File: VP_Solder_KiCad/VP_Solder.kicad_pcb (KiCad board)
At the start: 2 copper layers, 281 x 94.4 mm, 169 parts, among them J1 Conn_01x04, SW1 SW_Push, SW2 SW_Push, U1 STM32F072CBTx, U2 XC6206PxxxMR, U3 USBLC6-2SC6

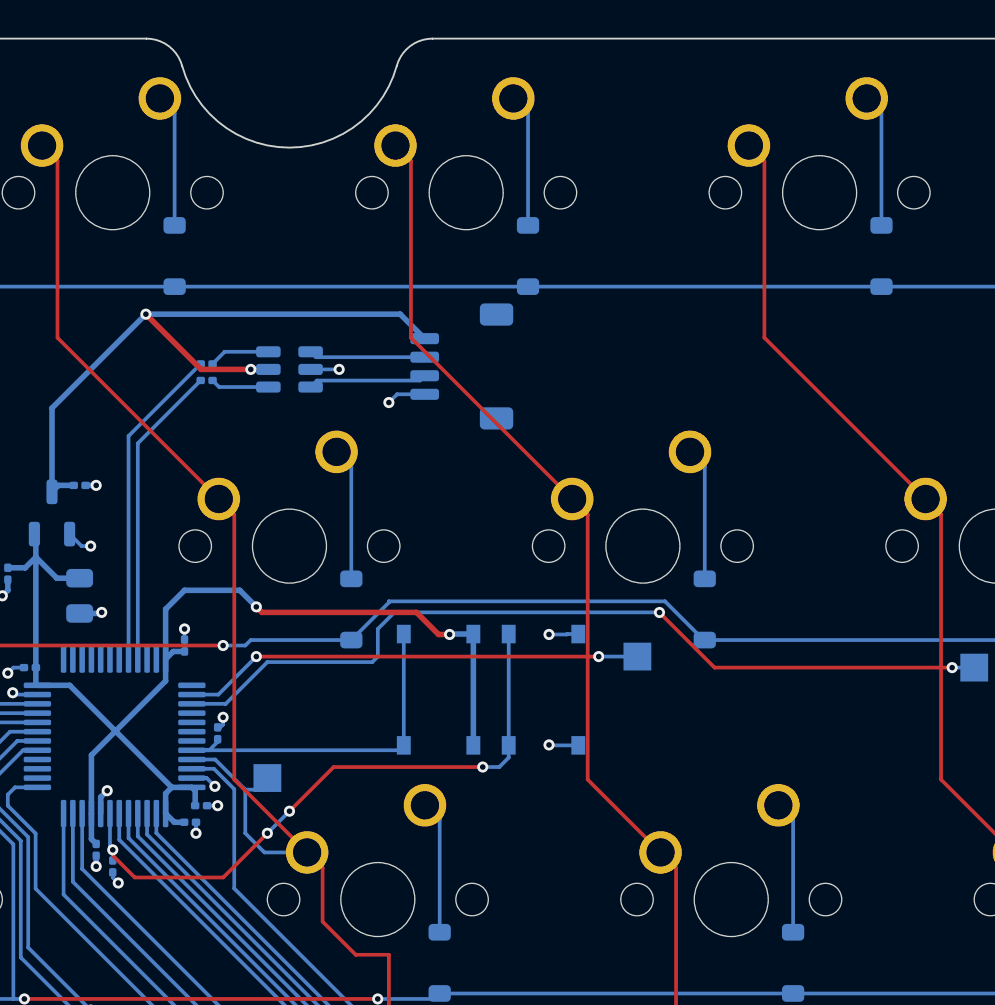
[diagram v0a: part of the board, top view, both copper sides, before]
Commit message: Small changes to silkscreen
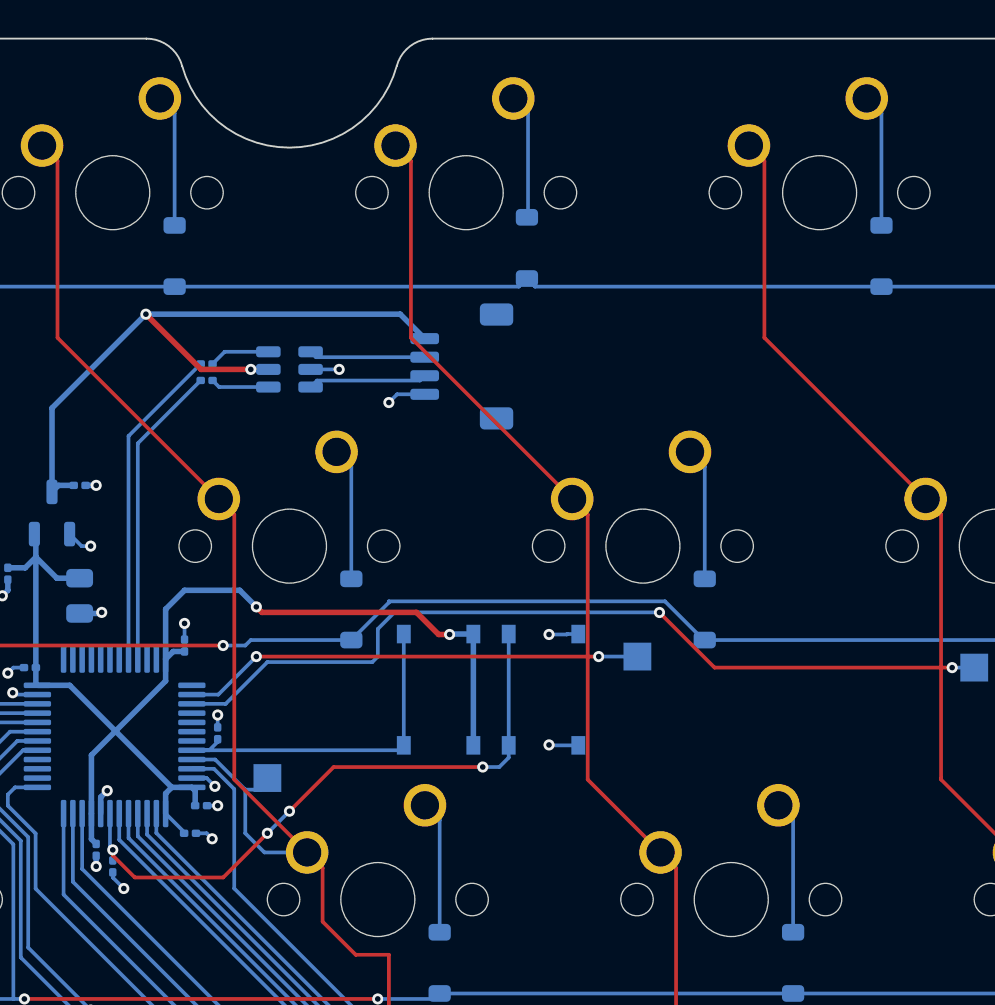
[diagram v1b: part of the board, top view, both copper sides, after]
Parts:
- added G***: LOGO, LOGO, B.Cu at (168.8, 151.3)
- moved C1 0.60 mm to (104.2, 113.0)
- moved D3 0.44 mm to (122.3, 81.4)
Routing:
- net GND: track 19.9 -> 21.0 mm
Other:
- board text added: "Firmware:"

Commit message: Changed testpoint names
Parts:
- renumbered TP2 to COL0, TP3 to COL1, TP12 to COL10, TP13 to COL11, TP14 to COL12, TP15 to COL13, TP4 to COL2, TP5 to COL3, TP6 to COL4, TP7 to COL5, TP8 to COL6, TP9 to COL7, TP10 to COL8, TP11 to COL9, TP1 to GND1
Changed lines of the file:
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@@
 		(descr "SMD rectangular pad as test Point, square 1.5mm side length")
 		(tags "test point SMD pad rectangle square")
-		(property "Reference" "TP4"
+		(property "Reference" "COL2"
 			(at 0 -1.785725 0)
 			(layer "B.SilkS")
@@
 		(descr "SMD rectangular pad as test Point, square 1.5mm side length")
 		(tags "test point SMD pad rectangle square")
-		(property "Reference" "TP3"
-			(at -2.381298 0.000203 0)
+		(property "Reference" "COL1"
+			(at -2.97656 0.000203 0)
 			(layer "B.SilkS")
 			(effects
@@
 		(descr "SMD rectangular pad as test Point, square 1.5mm side length")
 		(tags "test point SMD pad rectangle square")
-		(property "Reference" "TP13"
+		(property "Reference" "COL11"
 			(at -0.000337 -1.785762 0)
 			(layer "B.SilkS")
@@
 		(descr "SMD rectangular pad as test Point, square 1.5mm side length")
 		(tags "test point SMD pad rectangle square")
-		(property "Reference" "TP12"
+		(property "Reference" "COL10"
 			(at -0.000306 -1.785763 0)
 			(layer "B.SilkS")
@@
 		(descr "SMD rectangular pad as test Point, square 1.5mm side length")
 		(tags "test point SMD pad rectangle square")
-		(property "Reference" "TP14"
+		(property "Reference" "COL12"
 			(at 0 -1.785761 0)
 			(layer "B.SilkS")
@@
 		(descr "SMD rectangular pad as test Point, square 1.5mm side length")
 		(tags "test point SMD pad rectangle square")
-		(property "Reference" "TP10"
+		(property "Reference" "COL8"
 			(at -0.000244 -1.785765 0)
 			(layer "B.SilkS")
@@
 		(descr "SMD rectangular pad as test Point, square 1.5mm side length")
 		(tags "test point SMD pad rectangle square")
-		(property "Reference" "TP11"
+		(property "Reference" "COL9"
 			(at -0.000275 -1.785764 0)
 			(layer "B.SilkS")
@@
 		(descr "SMD rectangular pad as test Point, square 1.5mm side length")
 		(tags "test point SMD pad rectangle square")
-		(property "Reference" "TP6"
+		(property "Reference" "COL4"
 			(at 0 -1.785769 0)
 			(layer "B.SilkS")
@@
 		(descr "SMD rectangular pad as test Point, square 1.5mm side length")
 		(tags "test point SMD pad rectangle square")
-		(property "Reference" "TP8"
+		(property "Reference" "COL6"
 			(at 0 -1.785767 0)
 			(layer "B.SilkS")
@@
 				(name "A")
 				(pins "7" "44" "5" "6" "2" "3" "4" "18" "19" "20" "39" "40" "41" "42"
-					"43" "45" "46" "21" "22" "25" "26" "27" "28" "1" "24" "48" "23" "35"
+					"43" "45" "46" "21" "22" "25" "26" "27" "28" "1" "24" "48" "35" "23"
 					"47" "9" "8" "36" "10" "11" "12" "13" "14" "15" "16" "17" "29" "30"
 					"31" "32" "33" "34" "37" "38"
@@
 		(descr "SMD rectangular pad as test Point, square 1.5mm side length")
 		(tags "test point SMD pad rectangle square")
-		(property "Reference" "TP7"
+		(property "Reference" "COL5"
 			(at -0.000151 -1.785768 0)
 			(layer "B.SilkS")
@@
 		(descr "SMD rectangular pad as test Point, square 1.5mm side length")
 		(tags "test point SMD pad rectangle square")
-		(property "Reference" "TP2"
+		(property "Reference" "COL0"
 			(at 0 1.648 0)
 			(layer "B.SilkS")
@@
 		(descr "wire loop as test point, pitch 2.0mm, hole diameter 0.7mm, wire diameter 0.5mm")
 		(tags "test point wire loop")
-		(property "Reference" "TP1"
+		(property "Reference" "GND1"
 			(at 1.1 -1.7 0)
 			(layer "B.SilkS")
@@
 		(descr "SMD rectangular pad as test Point, square 1.5mm side length")
 		(tags "test point SMD pad rectangle square")
-		(property "Reference" "TP5"
+		(property "Reference" "COL3"
 			(at 0 -1.785726 0)
 			(layer "B.SilkS")
@@
 		(descr "SMD rectangular pad as test Point, square 1.5mm side length")
 		(tags "test point SMD pad rectangle square")
-		(property "Reference" "TP9"
+		(property "Reference" "COL7"
 			(at -0.000213 -1.785766 0)
 			(layer "B.SilkS")
@@
 		(descr "SMD rectangular pad as test Point, square 1.5mm side length")
 		(tags "test point SMD pad rectangle square")
-		(property "Reference" "TP15"
-			(at -0.5957 -1.78576 0)
+		(property "Reference" "COL13"
+			(at -0.892968 -1.78576 0)
 			(layer "B.SilkS")
 			(effects

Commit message: final changes, drc fixes
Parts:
- removed R2, R3: 22, Resistor_SMD:R_0201_0603Metric
- moved U3 3.31 mm to (112.8, 87.8)
- moved C8 2.45 mm to (96.7, 98.4), turned to 180 degrees
- moved C9 0.91 mm to (99.7, 113.9)
- moved COL2 0.89 mm to (127.4, 103.4)
- moved C6 0.84 mm to (97.6, 100.7), turned to 90 degrees
- moved D14 0.36 mm to (341.1, 81.8)
- moved C4 0.31 mm to (98.9, 113.7)
- moved J1 0.18 mm to (119.0, 87.8)
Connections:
- U1 pad 32: /RES_D- -> /ESD_D-
- U1 pad 33: /RES_D+ -> /ESD_D+
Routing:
- net /ESD_D-: track 3.28 -> 24.8 mm
- net /ESD_D+: track 3.15 -> 23.3 mm
- net /RES_D-: track 17.5 -> 0.00 mm
- net /RES_D+: track 16.4 -> 0.00 mm
- net /USB_D+: track 6.40 -> 3.20 mm
- net /USB_D-: track 6.27 -> 3.22 mm
- net +3.3V: track 67.2 -> 65.2 mm
- net /NRST: track 34.1 -> 32.4 mm
- net +5V: track 36.4 -> 35.4 mm
- net /COL2: track 115.6 -> 114.7 mm
- net GND: track 21.0 -> 21.6 mm, vias 18 -> 19
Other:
- board text added: "BOOT"
- board text added: "RESET"

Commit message: Cleaup
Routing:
- net GND: track 21.6 -> 22.1 mm
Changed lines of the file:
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@@
 	)
 	(via
-		(at 105.370292 113.24838)
+		(at 105.370292 112.653068)
 		(size 0.6)
 		(drill 0.3)
@@
 	)
 	(via
-		(at 116.085908 90.027217)
+		(at 116.383564 90.328868)
 		(size 0.6)
 		(drill 0.3)
@@
 	)
 	(via
-		(at 99.46266 110.569476)
+		(at 99.46266 110.59222)
 		(size 0.6)
 		(drill 0.3)
@@
 	)
 	(via
-		(at 99.119516 94.198396)
+		(at 99.417172 94.198396)
 		(size 0.6)
 		(drill 0.3)
@@
 	)
 	(segment
+		(start 116.978876 89.314867)
+		(end 117.008189 89.285554)
+		(width 0.3)
+		(layer "B.Cu")
+		(net "GND")
+	)
+	(segment
 		(start 97.058268 98.36558)
 		(end 97.928892 98.36558)
@@
 	)
 	(segment
-		(start 100.270507 114.73666)
+		(start 105.370292 112.653068)
+		(end 105.072636 112.950724)
+		(width 0.2)
+		(layer "B.Cu")
+		(net "GND")
+	)
+	(segment
+		(start 116.978876 89.733556)
+		(end 116.978876 89.314867)
+		(width 0.3)
+		(layer "B.Cu")
+		(net "GND")
+	)
+	(segment
+		(start 97.631236 99.796828)
+		(end 99.062484 99.796828)
+		(width 0.3)
+		(layer "B.Cu")
+		(net "GND")
+	)
+	(segment
+		(start 113.983978 87.76816)
+		(end 115.262764 87.76816)
+		(width 0.3)
+		(layer "B.Cu")
+		(net "GND")
+	)
+	(segment
+		(start 105.073595 109.975123)
+		(end 104.27516 109.975123)
+		(width 0.2)
+		(layer "B.Cu")
+		(net "GND")
+	)
+	(segment
+		(start 105.51912 110.420648)
+		(end 105.073595 109.975123)
+		(width 0.2)
+		(layer "B.Cu")
+		(net "GND")
+	)
+	(segment
+		(start 94.720475 105.475123)
+		(end 95.95016 105.475123)
+		(width 0.3)
+		(layer "B.Cu")
+		(net "GND")
+	)
+	(segment
+		(start 98.546548 94.198396)
+		(end 99.417172 94.198396)
+		(width 0.3)
+		(layer "B.Cu")
+		(net "GND")
+	)
+	(segment
+		(start 123.527308 102.235108)
+		(end 125.081212 102.235108)
+		(width 0.2)
+		(layer "B.Cu")
+		(net "GND")
+	)
+	(segment
+		(start 103.882012 102.51042)
+		(end 103.882012 101.639796)
+		(width 0.2)
+		(layer "B.Cu")
+		(net "GND")
+	)
+	(segment
+		(start 98.868533 114.352316)
+		(end 98.868533 113.978492)
+		(width 0.2)
+		(layer "B.Cu")
+		(net "GND")
+	)
+	(segment
+		(start 99.119516 114.603299)
+		(end 98.868533 114.352316)
+		(width 0.2)
+		(layer "B.Cu")
+		(net "GND")
+	)
+	(segment
+		(start 99.725211 114.469204)
 		(end 99.725211 114.191364)
 		(width 0.2)
-		(layer "B.Cu")
-		(net "GND")
-	)
-	(segment
-		(start 99.36266 111.887623)
-		(end 99.36266 110.669476)
-		(width 0.3)
 		(layer "B.Cu")
 		(net "GND")
@@
 	)
 	(segment
-		(start 97.631236 99.796828)
-		(end 99.062484 99.796828)
-		(width 0.3)
-		(layer "B.Cu")
-		(net "GND")
-	)
-	(segment
-		(start 113.983978 87.76816)
-		(end 115.262764 87.76816)
-		(width 0.3)
-		(layer "B.Cu")
-		(net "GND")
-	)
-	(segment
-		(start 105.073595 109.975123)
-		(end 104.27516 109.975123)
-		(width 0.2)
-		(layer "B.Cu")
-		(net "GND")
-	)
-	(segment
-		(start 105.51912 110.420648)
-		(end 105.073595 109.975123)
-		(width 0.2)
-		(layer "B.Cu")
-		(net "GND")
-	)
-	(segment
-		(start 94.720475 105.475123)
-		(end 95.95016 105.475123)
-		(width 0.3)
-		(layer "B.Cu")
-		(net "GND")
-	)
-	(segment
-		(start 123.527308 102.235108)
-		(end 125.081212 102.235108)
-		(width 0.2)
-		(layer "B.Cu")
-		(net "GND")
-	)
-	(segment
-		(start 100.607796 114.73666)
-		(end 100.270507 114.73666)
-		(width 0.2)
-		(layer "B.Cu")
-		(net "GND")
-	)
-	(segment
-		(start 103.882012 102.51042)
-		(end 103.882012 101.639796)
-		(width 0.2)
-		(layer "B.Cu")
-		(net "GND")
-	)
-	(segment
-		(start 98.868533 114.352316)
-		(end 98.868533 113.978492)
-		(width 0.2)
-		(layer "B.Cu")
-		(net "GND")
-	)
-	(segment
-		(start 99.119516 114.603299)
-		(end 98.868533 114.352316)
-		(width 0.2)
-		(layer "B.Cu")
-		(net "GND")
-	)
-	(segment
-		(start 105.370292 113.24838)
-		(end 105.072636 112.950724)
-		(width 0.2)
+		(start 116.383564 90.328868)
+		(end 116.978876 89.733556)
+		(width 0.3)
 		(layer "B.Cu")
 		(net "GND")
@@
 	)
 	(segment
+		(start 99.36266 110.669476)
+		(end 99.36266 111.887623)
+		(width 0.3)
+		(layer "B.Cu")
+		(net "GND")
+	)
+	(segment
 		(start 94.654676 104.021044)
 		(end 94.35702 104.3187)
@@
 	)
 	(segment
-		(start 98.546548 94.198396)
-		(end 99.119516 94.198396)
-		(width 0.3)
-		(layer "B.Cu")
-		(net "GND")
-	)
-	(segment
-		(start 116.085908 90.027217)
-		(end 116.827571 89.285554)
-		(width 0.3)
-		(layer "B.Cu")
-		(net "GND")
-	)
-	(segment
-		(start 99.36266 110.669476)
-		(end 99.46266 110.569476)
+		(start 99.992667 114.73666)
+		(end 99.725211 114.469204)
+		(width 0.2)
+		(layer "B.Cu")
+		(net "GND")
+	)
+	(segment
+		(start 99.439916 110.59222)
+		(end 99.36266 110.669476)
 		(width 0.3)
 		(layer "B.Cu")
@@
 	)
 	(segment
+		(start 99.46266 110.59222)
+		(end 99.439916 110.59222)
+		(width 0.3)
+		(layer "B.Cu")
+		(net "GND")
+	)
+	(segment
 		(start 102.096076 101.937452)
 		(end 102.36266 102.204036)
@@
 	)
 	(segment
-		(start 116.827571 89.285554)
-		(end 117.008189 89.285554)
-		(width 0.3)
-		(layer "B.Cu")
-		(net "GND")
+		(start 100.607796 114.73666)
+		(end 99.992667 114.73666)
+		(width 0.2)
+		(layer "B.Cu")
+		(net "GND")
